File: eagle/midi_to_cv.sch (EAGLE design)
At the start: 67 parts, among them IC1 TL082P, IC2 TL084P, IC4 TL082P, IC6 TL082P, IC7 TL082P, U1 ATMEGA328P_PDIP, U2 MCP4822-E/P, U3 MCP4822-E/P, U4 MCP4822-E/P, U5 MCP4822-E/P

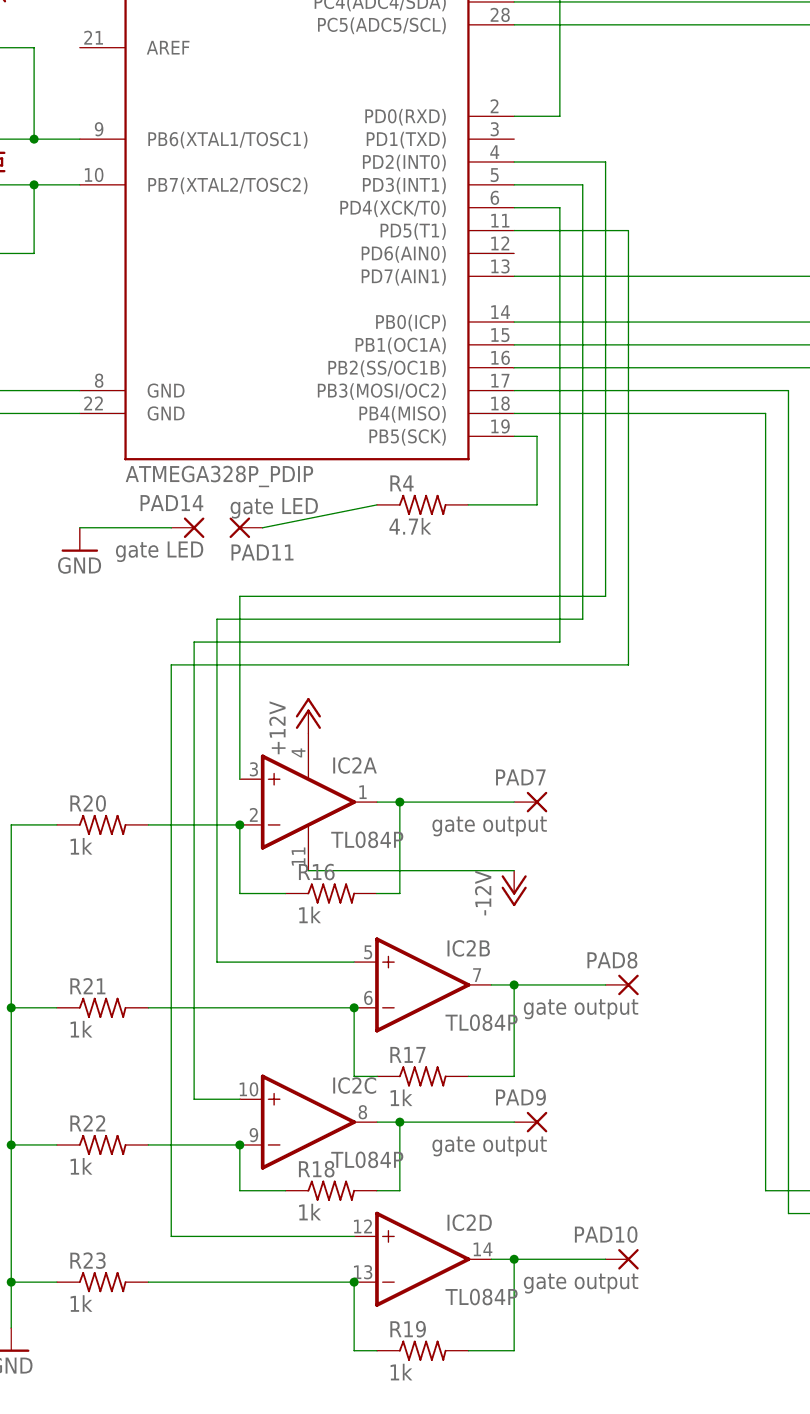
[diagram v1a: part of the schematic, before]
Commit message: routed with vias to gates
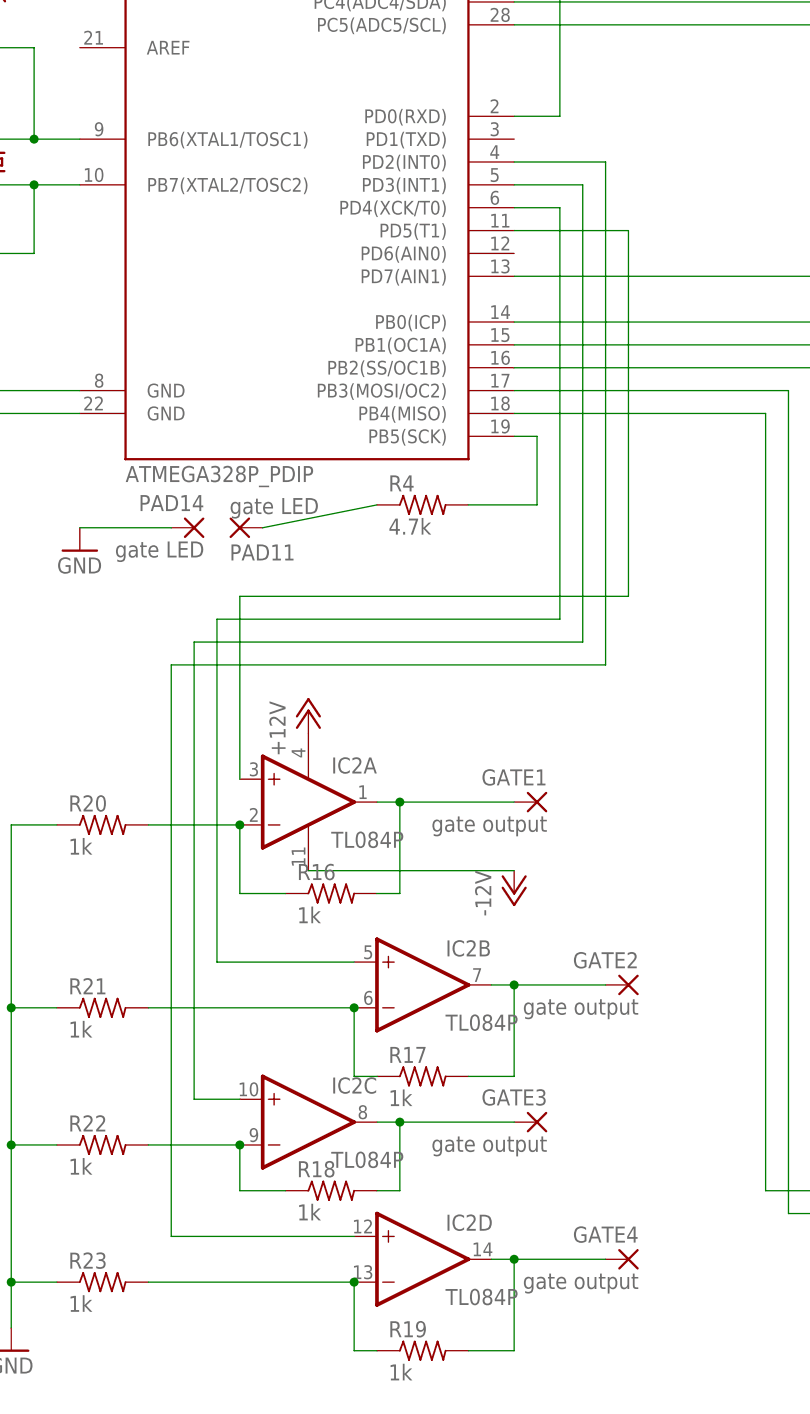
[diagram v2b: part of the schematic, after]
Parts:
- renumbered PAD10 to GATE4, PAD7 to GATE1, PAD8 to GATE2, PAD9 to GATE3
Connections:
- removed net N$34: IC2D.+IN, U1.PD5(T1)
- removed net N$44: IC2C.+IN, U1.PD4(XCK/T0)
- new net N$32: IC2A.+IN, U1.PD5(T1)
- new net N$33: IC2B.+IN, U1.PD4(XCK/T0)
- net N$45: now also IC2C.+IN; no longer IC2B.+IN
- net N$46: now also IC2D.+IN; no longer IC2A.+IN
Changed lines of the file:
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@@
 <part name="P+6" library="supply1" deviceset="+5V" device=""/>
 <part name="U4" library="MCP4822" deviceset="MCP4822-E/P" device=""/>
-<part name="PAD7" library="wirepad" deviceset="2,54/0,9" device="" value="gate output"/>
-<part name="PAD8" library="wirepad" deviceset="2,54/0,9" device="" value="gate output"/>
-<part name="PAD9" library="wirepad" deviceset="2,54/0,9" device="" value="gate output"/>
-<part name="PAD10" library="wirepad" deviceset="2,54/0,9" device="" value="gate output"/>
+<part name="GATE1" library="wirepad" deviceset="2,54/0,9" device="" value="gate output"/>
+<part name="GATE2" library="wirepad" deviceset="2,54/0,9" device="" value="gate output"/>
+<part name="GATE3" library="wirepad" deviceset="2,54/0,9" device="" value="gate output"/>
+<part name="GATE4" library="wirepad" deviceset="2,54/0,9" device="" value="gate output"/>
 <part name="IC2" library="linear" deviceset="TL084" device="P"/>
 <part name="PAD11" library="wirepad" deviceset="2,54/0,9" device="" value="gate LED"/>
@@
 <instance part="P+6" gate="1" x="109.22" y="-55.88"/>
 <instance part="U4" gate="A" x="129.54" y="-68.58"/>
-<instance part="PAD7" gate="1" x="45.72" y="-25.4" rot="MR0"/>
-<instance part="PAD8" gate="1" x="55.88" y="-45.72" rot="MR0"/>
-<instance part="PAD9" gate="1" x="45.72" y="-60.96" rot="MR0"/>
-<instance part="PAD10" gate="1" x="55.88" y="-76.2" rot="MR0"/>
+<instance part="GATE1" gate="1" x="45.72" y="-25.4" rot="MR0"/>
+<instance part="GATE2" gate="1" x="55.88" y="-45.72" rot="MR0"/>
+<instance part="GATE3" gate="1" x="45.72" y="-60.96" rot="MR0"/>
+<instance part="GATE4" gate="1" x="55.88" y="-76.2" rot="MR0"/>
 <instance part="IC2" gate="A" x="20.32" y="-25.4"/>
 <instance part="IC2" gate="B" x="33.02" y="-45.72"/>
@@
 </segment>
 </net>
-<net name="N$34" class="0">
-<segment>
-<pinref part="IC2" gate="D" pin="+IN"/>
-<wire x1="5.08" y1="-73.66" x2="25.4" y2="-73.66" width="0.1524" layer="91"/>
-<wire x1="5.08" y1="-73.66" x2="5.08" y2="-10.16" width="0.1524" layer="91"/>
-<wire x1="5.08" y1="-10.16" x2="55.88" y2="-10.16" width="0.1524" layer="91"/>
-<wire x1="55.88" y1="-10.16" x2="55.88" y2="38.1" width="0.1524" layer="91"/>
-<pinref part="U1" gate="G$1" pin="PD5(T1)"/>
-<wire x1="55.88" y1="38.1" x2="43.18" y2="38.1" width="0.1524" layer="91"/>
-</segment>
-</net>
 <net name="N$35" class="0">
 <segment>
 <pinref part="IC2" gate="A" pin="OUT"/>
-<pinref part="PAD7" gate="1" pin="P"/>
+<pinref part="GATE1" gate="1" pin="P"/>
 <wire x1="27.94" y1="-25.4" x2="30.48" y2="-25.4" width="0.1524" layer="91"/>
 <pinref part="R16" gate="G$1" pin="2"/>
@@
 <segment>
 <pinref part="IC2" gate="B" pin="OUT"/>
-<pinref part="PAD8" gate="1" pin="P"/>
+<pinref part="GATE2" gate="1" pin="P"/>
 <wire x1="40.64" y1="-45.72" x2="43.18" y2="-45.72" width="0.1524" layer="91"/>
 <pinref part="R17" gate="G$1" pin="2"/>
@@
 <segment>
 <pinref part="IC2" gate="C" pin="OUT"/>
-<pinref part="PAD9" gate="1" pin="P"/>
+<pinref part="GATE3" gate="1" pin="P"/>
 <wire x1="27.94" y1="-60.96" x2="30.48" y2="-60.96" width="0.1524" layer="91"/>
 <pinref part="R18" gate="G$1" pin="2"/>
@@
 <segment>
 <pinref part="IC2" gate="D" pin="OUT"/>
-<pinref part="PAD10" gate="1" pin="P"/>
+<pinref part="GATE4" gate="1" pin="P"/>
 <wire x1="40.64" y1="-76.2" x2="43.18" y2="-76.2" width="0.1524" layer="91"/>
 <pinref part="R19" gate="G$1" pin="2"/>
@@
 </segment>
 </net>
-<net name="N$44" class="0">
-<segment>
+<net name="N$45" class="0">
+<segment>
+<pinref part="U1" gate="G$1" pin="PD3(INT1)"/>
+<wire x1="43.18" y1="43.18" x2="50.8" y2="43.18" width="0.1524" layer="91"/>
+<wire x1="50.8" y1="43.18" x2="50.8" y2="-7.62" width="0.1524" layer="91"/>
 <pinref part="IC2" gate="C" pin="+IN"/>
 <wire x1="7.62" y1="-58.42" x2="12.7" y2="-58.42" width="0.1524" layer="91"/>
-<pinref part="U1" gate="G$1" pin="PD4(XCK/T0)"/>
-<wire x1="43.18" y1="40.64" x2="48.26" y2="40.64" width="0.1524" layer="91"/>
-<wire x1="48.26" y1="40.64" x2="48.26" y2="-7.62" width="0.1524" layer="91"/>
-<wire x1="48.26" y1="-7.62" x2="7.62" y2="-7.62" width="0.1524" layer="91"/>
 <wire x1="7.62" y1="-7.62" x2="7.62" y2="-58.42" width="0.1524" layer="91"/>
-</segment>
-</net>
-<net name="N$45" class="0">
-<segment>
-<pinref part="IC2" gate="B" pin="+IN"/>
-<pinref part="U1" gate="G$1" pin="PD3(INT1)"/>
-<wire x1="10.16" y1="-43.18" x2="25.4" y2="-43.18" width="0.1524" layer="91"/>
-<wire x1="43.18" y1="43.18" x2="50.8" y2="43.18" width="0.1524" layer="91"/>
-<wire x1="50.8" y1="43.18" x2="50.8" y2="-5.08" width="0.1524" layer="91"/>
-<wire x1="50.8" y1="-5.08" x2="10.16" y2="-5.08" width="0.1524" layer="91"/>
-<wire x1="10.16" y1="-5.08" x2="10.16" y2="-43.18" width="0.1524" layer="91"/>
+<wire x1="50.8" y1="-7.62" x2="7.62" y2="-7.62" width="0.1524" layer="91"/>
 </segment>
 </net>
 <net name="N$46" class="0">
 <segment>
-<pinref part="IC2" gate="A" pin="+IN"/>
 <pinref part="U1" gate="G$1" pin="PD2(INT0)"/>
 <wire x1="43.18" y1="45.72" x2="53.34" y2="45.72" width="0.1524" layer="91"/>
-<wire x1="53.34" y1="45.72" x2="53.34" y2="-2.54" width="0.1524" layer="91"/>
-<wire x1="53.34" y1="-2.54" x2="12.7" y2="-2.54" width="0.1524" layer="91"/>
-<wire x1="12.7" y1="-2.54" x2="12.7" y2="-22.86" width="0.1524" layer="91"/>
+<wire x1="53.34" y1="45.72" x2="53.34" y2="-10.16" width="0.1524" layer="91"/>
+<pinref part="IC2" gate="D" pin="+IN"/>
+<wire x1="5.08" y1="-73.66" x2="25.4" y2="-73.66" width="0.1524" layer="91"/>
+<wire x1="5.08" y1="-73.66" x2="5.08" y2="-10.16" width="0.1524" layer="91"/>
+<wire x1="53.34" y1="-10.16" x2="5.08" y2="-10.16" width="0.1524" layer="91"/>
 </segment>
 </net>
@@
 </segment>
 </net>
+<net name="N$32" class="0">
+<segment>
+<pinref part="IC2" gate="A" pin="+IN"/>
+<wire x1="12.7" y1="-2.54" x2="12.7" y2="-22.86" width="0.1524" layer="91"/>
+<pinref part="U1" gate="G$1" pin="PD5(T1)"/>
+<wire x1="55.88" y1="38.1" x2="43.18" y2="38.1" width="0.1524" layer="91"/>
+<wire x1="12.7" y1="-2.54" x2="55.88" y2="-2.54" width="0.1524" layer="91"/>
+<wire x1="55.88" y1="-2.54" x2="55.88" y2="38.1" width="0.1524" layer="91"/>
+</segment>
+</net>
+<net name="N$33" class="0">
+<segment>
+<pinref part="U1" gate="G$1" pin="PD4(XCK/T0)"/>
+<wire x1="43.18" y1="40.64" x2="48.26" y2="40.64" width="0.1524" layer="91"/>
+<wire x1="48.26" y1="40.64" x2="48.26" y2="-5.08" width="0.1524" layer="91"/>
+<pinref part="IC2" gate="B" pin="+IN"/>
+<wire x1="10.16" y1="-43.18" x2="25.4" y2="-43.18" width="0.1524" layer="91"/>
+<wire x1="10.16" y1="-5.08" x2="10.16" y2="-43.18" width="0.1524" layer="91"/>
+<wire x1="48.26" y1="-5.08" x2="10.16" y2="-5.08" width="0.1524" layer="91"/>
+</segment>
+</net>
